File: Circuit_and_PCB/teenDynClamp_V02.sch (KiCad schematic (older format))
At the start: 35 parts, among them J1 12V DC, J2 VIN, J3 VDAQ, J4 VAMP, J5 TTL, J6 Breakout, SW1 Power Switch, U1 TLE2426xP, U2 LP2950-3.3, U3 AD8031ANZ, U4 Teensy3.6, U5 LM358

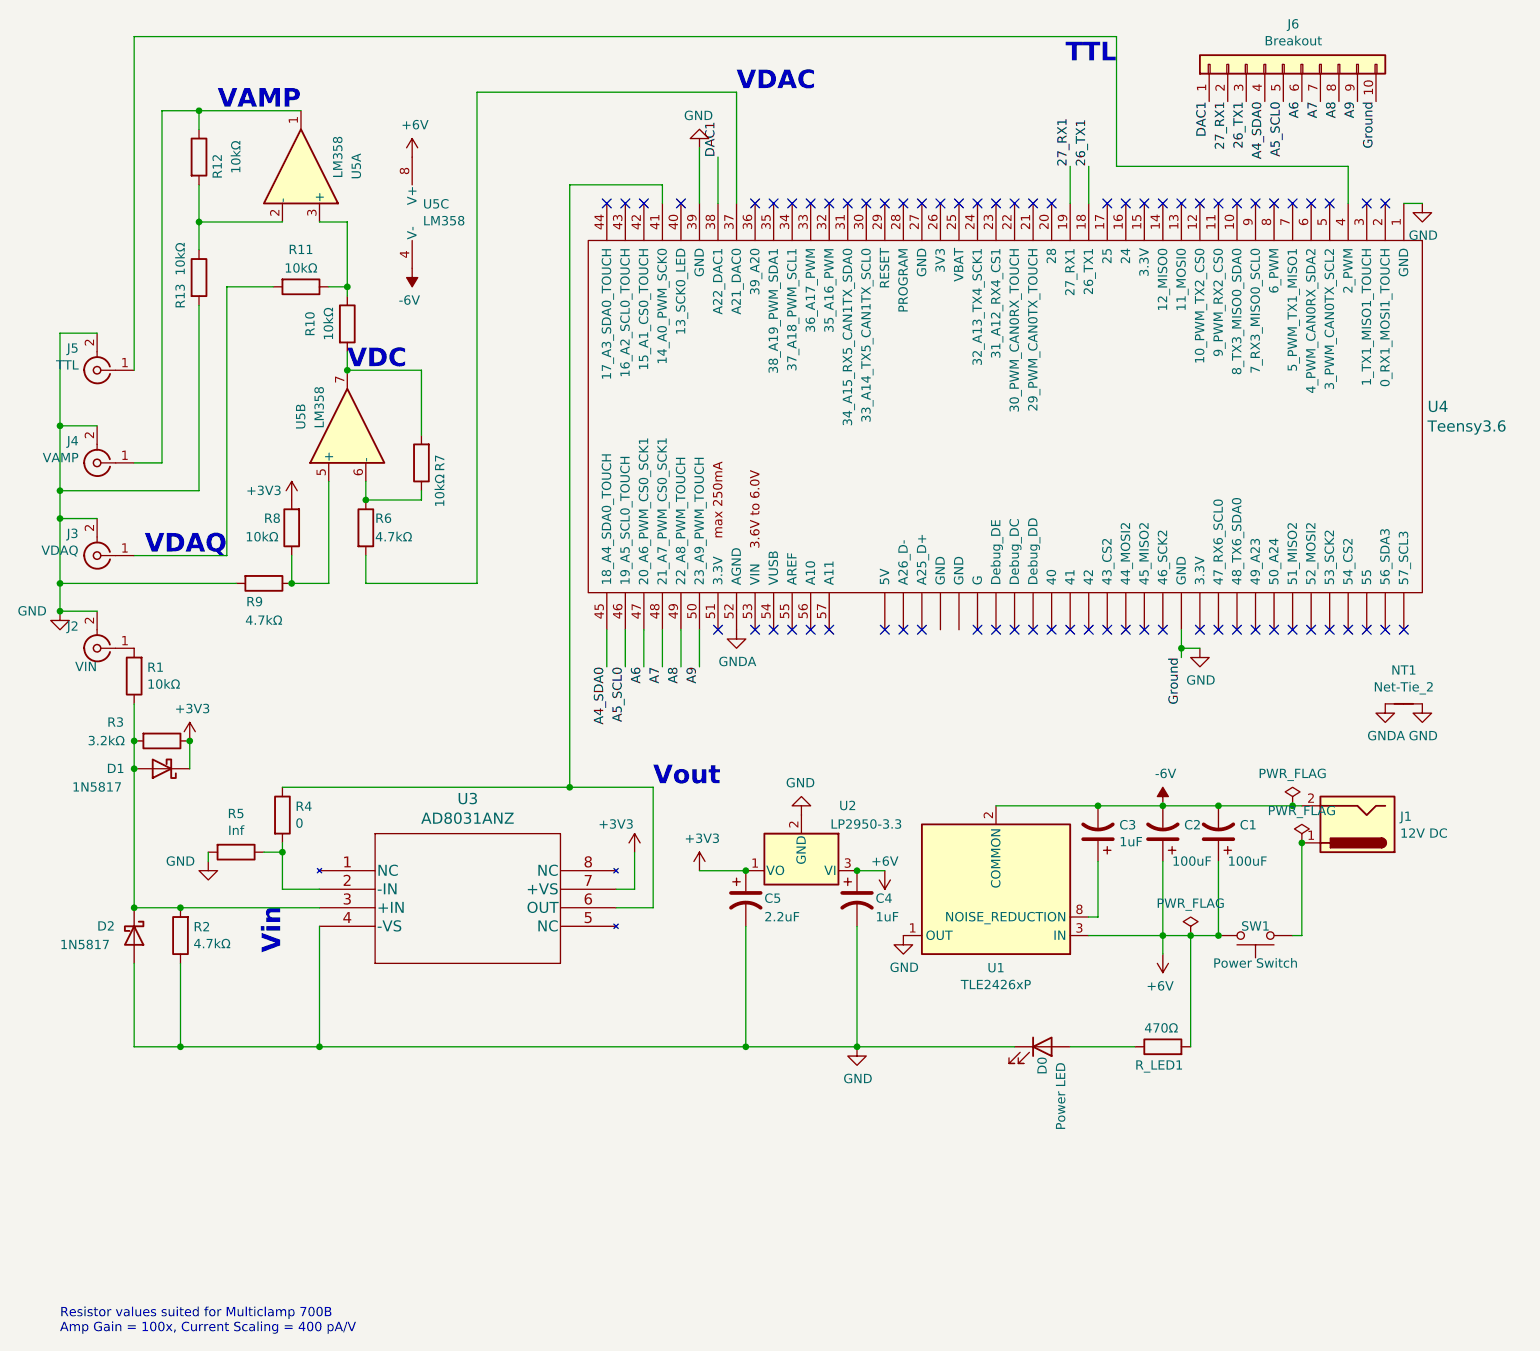
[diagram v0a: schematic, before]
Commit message: Added Mode toggle and TTL Safety
As suggested by Niraj, added two more features to the design:
1. A 0.5x voltage divider to protect teensy from TTL voltages above 3.3V.
2. Added a toggle switch which can either bypass the dynamic clamp. Switch footprint is of a pin-header where any dual pole dual throw switch can be soldered. There are indicator LEDs to show which mode the dynClamp is in.
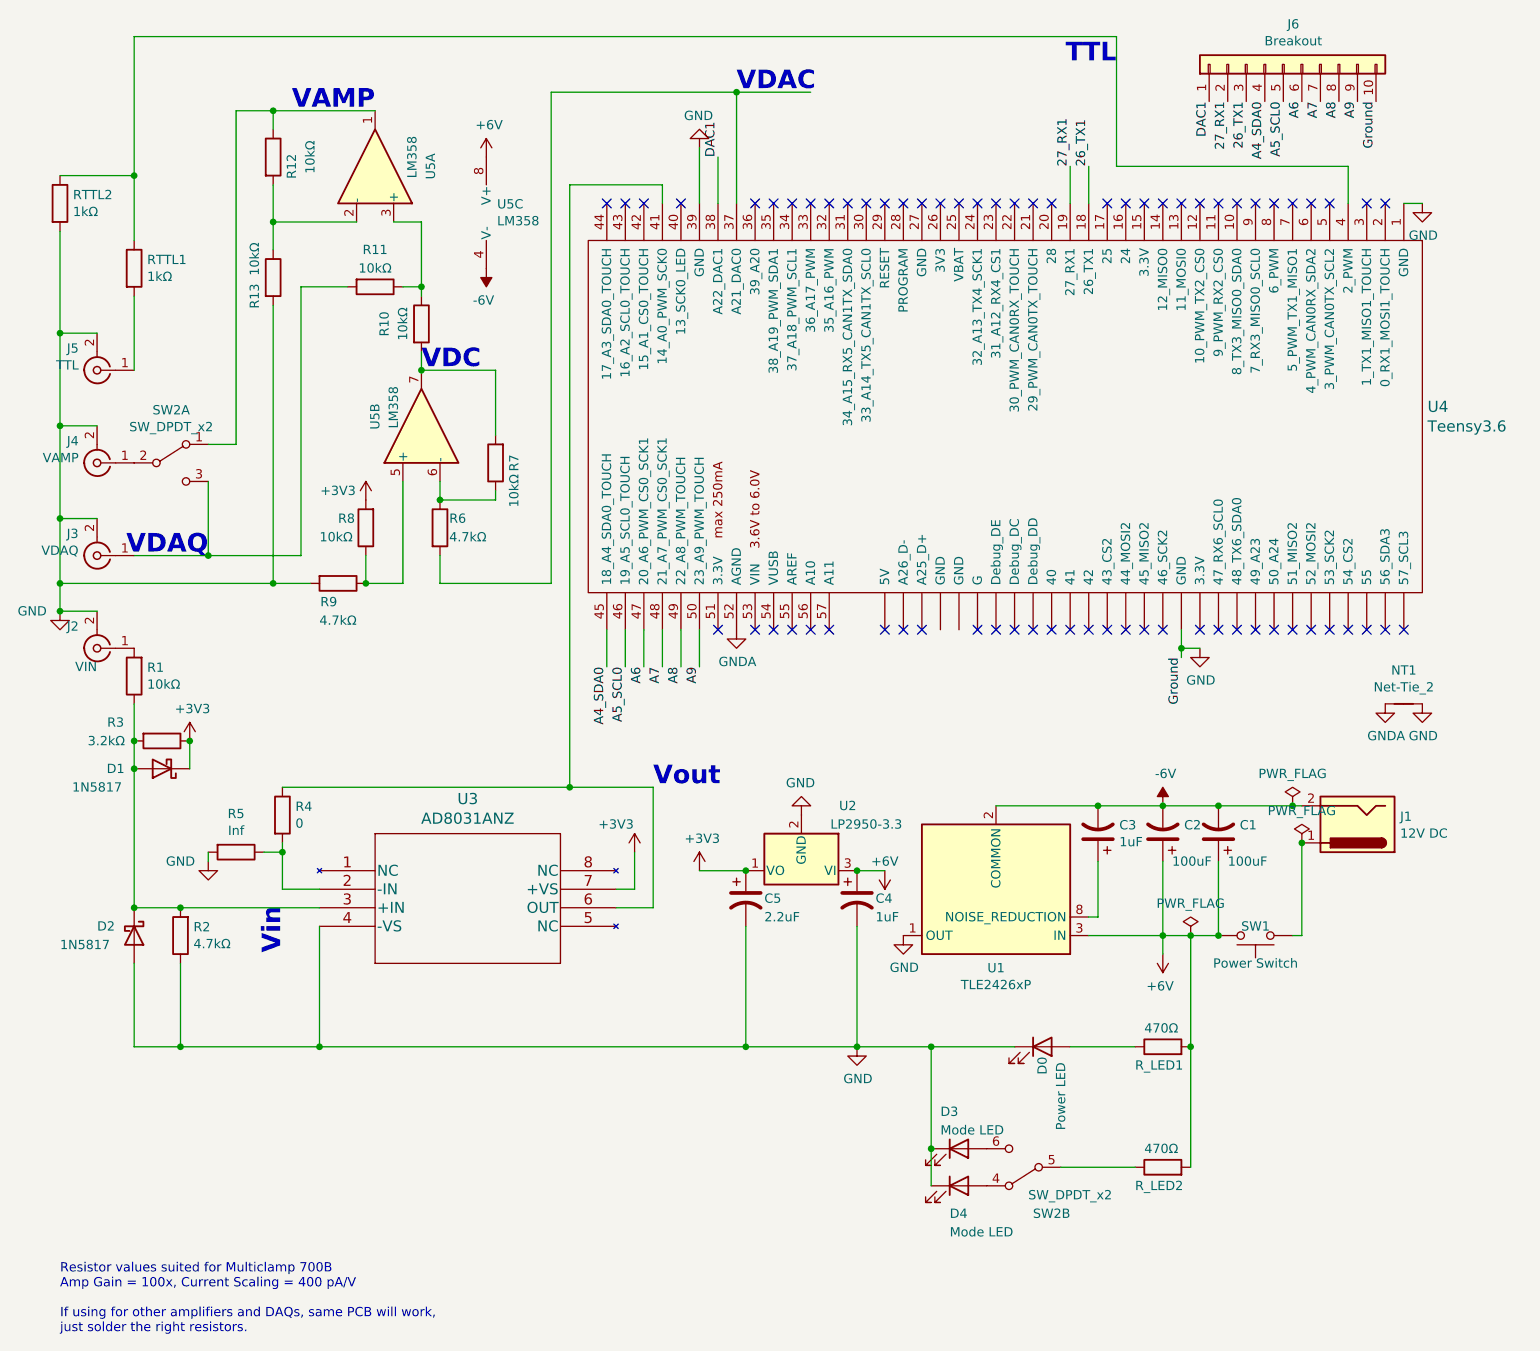
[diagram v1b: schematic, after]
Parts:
- removed U3: AD8031ANZ, Package_DIP:DIP-8_W7.62mm, symbol ad8031anz_pinCorrected:AD8031ANZ
- added D3, D4: Mode LED, LED_THT:LED_D3.0mm, symbol Device:LED
- added RTTL1, RTTL2: 1kΩ, Resistor_THT:R_Axial_DIN0207_L6.3mm_D2.5mm_P7.62mm_Horizontal, symbol Device:R
- added R_LED2: 470Ω, Resistor_THT:R_Axial_DIN0207_L6.3mm_D2.5mm_P7.62mm_Horizontal, symbol Device:R
- added SW2: SW_DPDT_x2, dynClamp:PinHeader_2x03_P2.54mm_Vertical_row_wise, symbol Switch:SW_DPDT_x2
- added U3: AD8031ANZ, Package_DIP:DIP-8_W7.62mm, symbol dynClamp:AD8031ANZ
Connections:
- net +3V3: now also U3.7 (+VS)
- net +6V: now also R_LED2.2
- net GND: now also D3.1 (K), D4.1 (K), RTTL2.2, U3.4 (-VS)
- net at J3.1 (In), R11.2: now also SW2.3 (C)
- net at R12.1, U5.1: now also SW2.1 (A); no longer J4.1 (In)
- net at R4.2, R5.1: now also U3.2 (-IN)
- net at D1.2 (A), D2.1 (K), R1.1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: now also U3.3 (+IN)
- net at R4.1, U4.41 (14_A0_PWM_SCK0): now also U3.6 (OUT)
- net at J5.1 (In): now also RTTL1.2; no longer U4.4 (2_PWM)
- new net: J4.1 (In), SW2.2 (B)
- new net: RTTL1.1, RTTL2.1, U4.4 (2_PWM)
- new net: D4.2 (A), SW2.4 (A)
- new net: R_LED2.1, SW2.5 (B)
- new net: D3.2 (A), SW2.6 (C)
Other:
- note added: "Resistor values suited for Multiclamp 700B\nAmp Gain = 100x, Current Scaling = 400 pA/V\n\nIf using for other amplifiers and DAQs, same PCB will work,\njust solder the right resistors."
- note removed: "Resistor values suited for Multiclamp 700B\nAmp Gain = 100x, Current Scaling = 400 pA/V"
- moved on the sheet: R10, R11, R12, R13, R6, R7, R8, R9, U5A, U5B, U5C

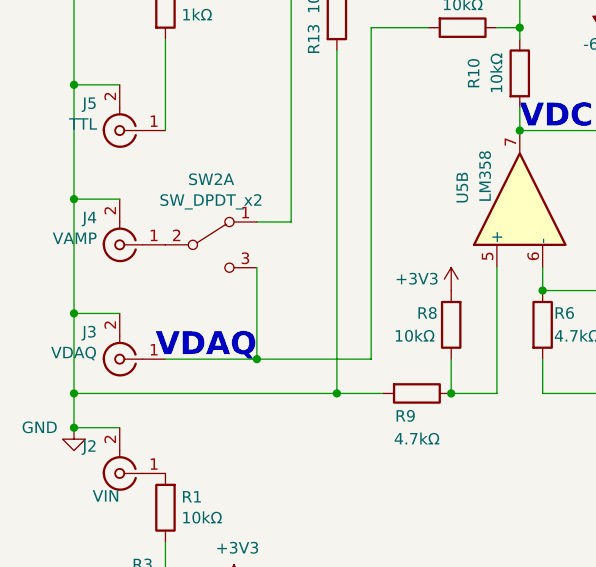
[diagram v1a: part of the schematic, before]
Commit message: Added pulldown resistor
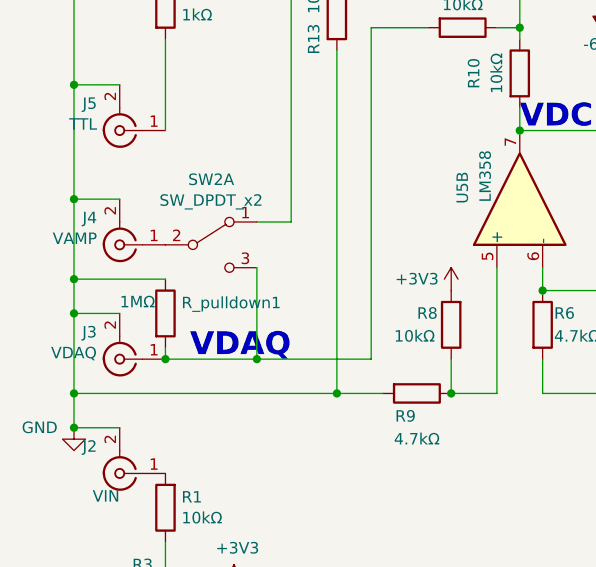
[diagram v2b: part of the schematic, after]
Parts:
- added R_pulldown1: 1MΩ, Resistor_THT:R_Axial_DIN0207_L6.3mm_D2.5mm_P7.62mm_Horizontal, symbol Device:R
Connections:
- net GND: now also R_pulldown1.1
- net at J3.1 (In), R11.2, SW2.3 (C): now also R_pulldown1.2
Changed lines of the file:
@@
 Text Notes 2750 2500 0    100  ~ 20
 VDC
-Text Notes 1600 3500 2    100  ~ 20
+Text Notes 1750 3500 2    100  ~ 20
 VDAQ
 Text Notes 2500 1100 2    100  ~ 20
@@
 Wire Wire Line
 	800  3300 800  3650
-Wire Wire Line
-	800  2800 800  3300
-Wire Wire Line
-	800  3650 1950 3650
 Connection ~ 800  3650
 Wire Wire Line
@@
 	1600 3100 1600 3500
 Connection ~ 1600 3500
-Wire Wire Line
-	1600 3500 2100 3500
 $Comp
 L Device:R RTTL2
@@
 	1    0    0    -1
 $EndComp
+Wire Wire Line
+	1600 3500 2100 3500
+Wire Wire Line
+	800  3650 1950 3650
+$Comp
+L Device:R R_pulldown1
+U 1 1 5F5A4F55
+P 1200 3300
+F 0 "R_pulldown1" H 1270 3346 50  0000 L CNN
+F 1 "1MΩ" H 1000 3350 50  0000 L CNN
+F 2 "Resistor_THT:R_Axial_DIN0207_L6.3mm_D2.5mm_P7.62mm_Horizontal" V 1130 3300 50  0001 C CNN
+F 3 "~" H 1200 3300 50  0001 C CNN
+	1    1200 3300
+	1    0    0    -1
+$EndComp
+Wire Wire Line
+	1200 3150 800  3150
+Wire Wire Line
+	800  2800 800  3150
+Connection ~ 800  3150
+Wire Wire Line
+	800  3150 800  3300
+Wire Wire Line
+	1200 3450 1200 3500
+Connection ~ 1200 3500
 $EndSCHEMATC
